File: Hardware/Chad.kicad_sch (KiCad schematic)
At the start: 39 parts, among them J1 RBUS, J2 GPIO Breakout, J3 ServoCH1, J4 ServoCH2, U1 ESP32-S3, Y1 40MHz±10ppm

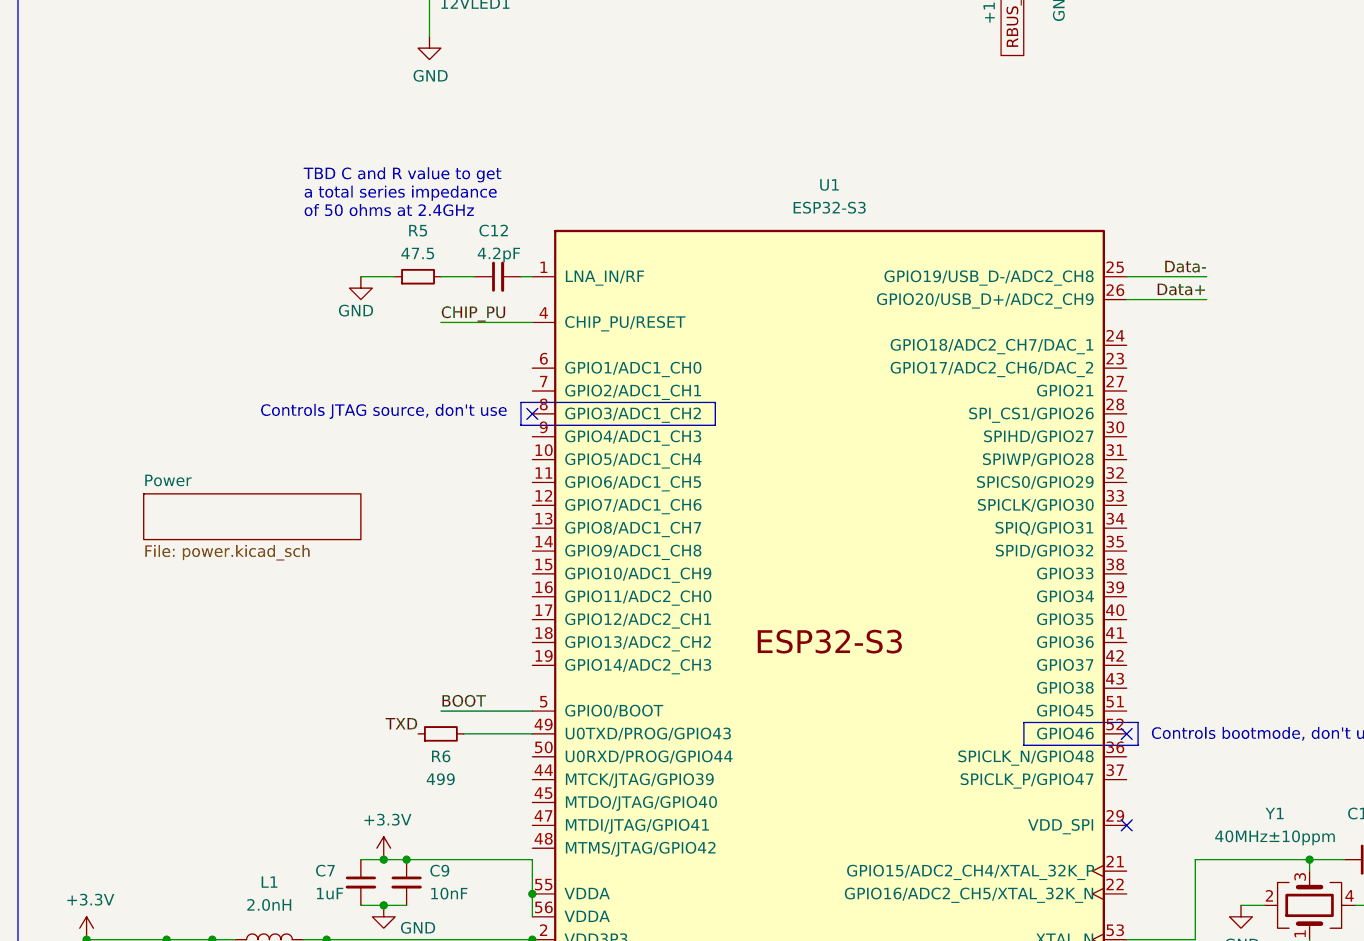
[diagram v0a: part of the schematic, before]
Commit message: Mostly completed RBUS side, still buck converter side to do
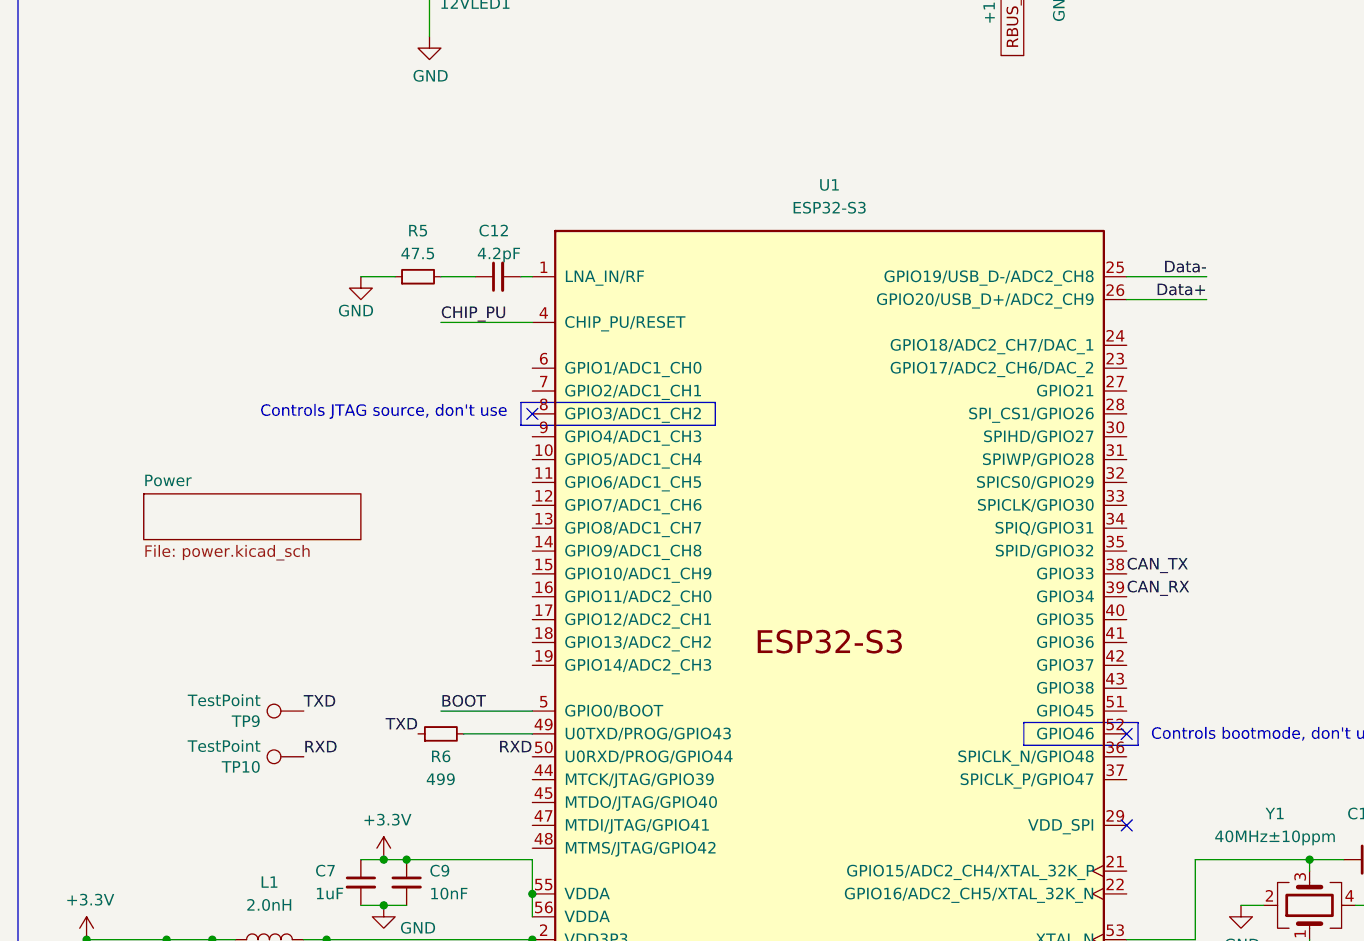
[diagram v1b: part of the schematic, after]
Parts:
- added TP10, TP9: TestPoint, TestPoint:TestPoint_Pad_D1.0mm, symbol Connector:TestPoint
- 12VLED1, 3V3LED1, TXLED1: footprint Resistor_SMD:R_0402_1005Metric -> LED_SMD:LED_0402_1005Metric
- J2: footprint (none) -> Connector_PinSocket_2.54mm:PinSocket_2x04_P2.54mm_Vertical
- U1: footprint Package_DFN_QFN:QFN-56-1EP_7x7mm_P0.4mm_EP5.6x5.6mm -> iclr:QFN40P700X700X90-57N
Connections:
- net CAN_RX: now also U1.39 (GPIO34)
- net CAN_TX: now also U1.38 (GPIO33)
- net TXD: now also TP9.1
- net RXD: now reaches U1.50 (U0RXD/PROG/GPIO44)
- net RXD: now also TP10.1
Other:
- note removed: "TBD C and R value to get a total series impedance of 50 ohms at 2.4GHz"
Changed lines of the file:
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@@
-    (effects (font (size 1.27 1.27)) (justify left bottom))
-  )
-  (text "TBD C and R value to get\na total series impedance\nof 50 ohms at 2.4GHz\n"
-    (at 44.45 55.88 0)
     (effects (font (size 1.27 1.27)) (justify left bottom))
   )
@@
     (effects (font (size 1.27 1.27)) (justify right bottom))
   )
+  (label "TXD" (at 44.45 110.49 0)
+    (effects (font (size 1.27 1.27)) (justify left bottom))
+  )
   (label "GPIO0" (at 270.51 105.41 180)
     (effects (font (size 1.27 1.27)) (justify right bottom))
@@
   (label "CHIP_PU" (at 36.83 165.1 180)
     (effects (font (size 1.27 1.27)) (justify right bottom))
+  )
+  (label "RXD" (at 44.45 115.57 0)
+    (effects (font (size 1.27 1.27)) (justify left bottom))
   )
   (label "Servo2PWM" (at 271.78 90.17 180)
@@
     (effects (font (size 1.27 1.27)) (justify right bottom))
   )
+  (label "CAN_TX" (at 135.89 95.25 0)
+    (effects (font (size 1.27 1.27)) (justify left bottom))
+  )
   (label "CHIP_PU" (at 59.69 67.31 0)
     (effects (font (size 1.27 1.27)) (justify left bottom))
   )
+  (label "RXD" (at 69.85 115.57 180)
+    (effects (font (size 1.27 1.27)) (justify right bottom))
+  )
   (label "CAN_RX" (at 115.57 182.88 0)
     (effects (font (size 1.27 1.27)) (justify left bottom))
@@
   (label "Data-" (at 144.78 62.23 180)
     (effects (font (size 1.27 1.27)) (justify right bottom))
+  )
+  (label "CAN_RX" (at 135.89 97.79 0)
+    (effects (font (size 1.27 1.27)) (justify left bottom))
   )
   (label "Servo1PWM" (at 271.78 74.93 180)
@@
     (property "Reference" "TXLED1" (id 0) (at 25.4 26.797 0))
     (property "Value" "TX_LED" (id 1) (at 25.4 24.4856 0))
-    (property "Footprint" "Resistor_SMD:R_0402_1005Metric" (id 2) (at 25.4 21.59 90)
+    (property "Footprint" "LED_SMD:LED_0402_1005Metric" (id 2) (at 25.4 21.59 90)
       (effects (font (size 1.27 1.27)) hide)
     )
@@
     (property "Reference" "3V3LED1" (id 0) (at 54.61 16.383 0))
     (property "Value" "3V3LED" (id 1) (at 54.61 18.6944 0))
-    (property "Footprint" "Resistor_SMD:R_0402_1005Metric" (id 2) (at 54.61 21.59 90)
+    (property "Footprint" "LED_SMD:LED_0402_1005Metric" (id 2) (at 54.61 21.59 90)
       (effects (font (size 1.27 1.27)) hide)
     )
@@
     (property "Reference" "12VLED1" (id 0) (at 63.5 31.877 0))
     (property "Value" "12V_LED" (id 1) (at 63.5 29.5656 0))
-    (property "Footprint" "Resistor_SMD:R_0402_1005Metric" (id 2) (at 63.5 26.67 90)
+    (property "Footprint" "LED_SMD:LED_0402_1005Metric" (id 2) (at 63.5 26.67 90)
       (effects (font (size 1.27 1.27)) hide)
     )
@@
       (effects (font (size 1.27 1.27)) (justify left))
     )
-    (property "Footprint" "" (id 2) (at 275.59 113.03 0)
+    (property "Footprint" "Connector_PinSocket_2.54mm:PinSocket_2x04_P2.54mm_Vertical" (id 2) (at 275.59 113.03 0)
       (effects (font (size 1.27 1.27)) hide)
     )
@@
     (pin "1")
   )
+  (symbol (lib_id "Connector:TestPoint") (at 44.45 110.49 90) (unit 1)
+    (in_bom yes) (on_board yes)
+    (property "Reference" "TP9" (id 0) (at 39.6748 111.6584 90)
+      (effects (font (size 1.27 1.27)) (justify left))
+    )
+    (property "Value" "TestPoint" (id 1) (at 39.6748 109.347 90)
+      (effects (font (size 1.27 1.27)) (justify left))
+    )
+    (property "Footprint" "TestPoint:TestPoint_Pad_D1.0mm" (id 2) (at 44.45 105.41 0)
+      (effects (font (size 1.27 1.27)) hide)
+    )
+    (property "Datasheet" "~" (id 3) (at 44.45 105.41 0)
+      (effects (font (size 1.27 1.27)) hide)
+    )
+    (pin "1")
+  )
   (symbol (lib_id "power:+12V") (at 120.65 25.4 180) (unit 1)
     (in_bom yes) (on_board yes)
@@
     (pin "1")
     (pin "2")
+  )
+  (symbol (lib_id "Connector:TestPoint") (at 44.45 115.57 90) (unit 1)
+    (in_bom yes) (on_board yes)
+    (property "Reference" "TP10" (id 0) (at 39.6748 116.7384 90)
+      (effects (font (size 1.27 1.27)) (justify left))
+    )
+    (property "Value" "TestPoint" (id 1) (at 39.6748 114.427 90)
+      (effects (font (size 1.27 1.27)) (justify left))
+    )
+    (property "Footprint" "TestPoint:TestPoint_Pad_D1.0mm" (id 2) (at 44.45 110.49 0)
+      (effects (font (size 1.27 1.27)) hide)
+    )
+    (property "Datasheet" "~" (id 3) (at 44.45 110.49 0)
+      (effects (font (size 1.27 1.27)) hide)
+    )
+    (pin "1")
   )
   (symbol (lib_id "Device:C_Small") (at 162.56 127 90) (unit 1)
@@
     (property "Reference" "U1" (id 0) (at 102.87 52.07 0))
     (property "Value" "ESP32-S3" (id 1) (at 102.87 54.61 0))
-    (property "Footprint" "Package_DFN_QFN:QFN-56-1EP_7x7mm_P0.4mm_EP5.6x5.6mm" (id 2) (at 102.87 153.67 0)
+    (property "Footprint" "iclr:QFN40P700X700X90-57N" (id 2) (at 102.87 153.67 0)
       (effects (font (size 1.27 1.27)) hide)
     )
@@
     )
     (path "/00000000-0000-0000-0000-00005dc1f7e5"
-      (reference "3V3LED1") (unit 1) (value "3V3LED") (footprint "Resistor_SMD:R_0402_1005Metric")
+      (reference "3V3LED1") (unit 1) (value "3V3LED") (footprint "LED_SMD:LED_0402_1005Metric")
     )
     (path "/00000000-0000-0000-0000-000061b674e8"
-      (reference "12VLED1") (unit 1) (value "12V_LED") (footprint "Resistor_SMD:R_0402_1005Metric")
+      (reference "12VLED1") (unit 1) (value "12V_LED") (footprint "LED_SMD:LED_0402_1005Metric")
     )
     (path "/00000000-0000-0000-0000-00005dff8440"
@@
     )
     (path "/00000000-0000-0000-0000-000061942b9a/c905e3f6-13b1-4d5f-8bb5-930cfa107996"
-      (reference "C17") (unit 1) (value "0.1uF") (footprint "Capacitor_SMD:C_0402_1005Metric")
+      (reference "C17") (unit 1) (value "47nF") (footprint "Capacitor_SMD:C_0402_1005Metric")
     )
     (path "/00000000-0000-0000-0000-000061942b9a/23622c20-4a70-4ee7-b39c-f5519633413f"
@@
     )
     (path "/4787afbf-a567-4e80-9253-fc8002fdff49"
-      (reference "J2") (unit 1) (value "GPIO Breakout") (footprint "")
+      (reference "J2") (unit 1) (value "GPIO Breakout") (footprint "Connector_PinSocket_2.54mm:PinSocket_2x04_P2.54mm_Vertical")
     )
     (path "/0f659bd2-aada-46fb-8f2b-6d45cea3ad46"
@@
     )
     (path "/00000000-0000-0000-0000-000061942b9a/deb2b25e-9fb0-448e-88c5-95a67db1d371"
-      (reference "JP1") (unit 1) (value "TermJP") (footprint "Jumper:SolderJumper-2_P1.3mm_Open_RoundedPad1.0x1.5mm")
+      (reference "JP1") (unit 1) (value "TermJP") (footprint "iclr:SmallerSolderJP")
     )
     (path "/c6e654d3-0d45-4a74-8557-db0239fe22b2"
@@
     )
     (path "/00000000-0000-0000-0000-000061942b9a/c4e42d16-8dbe-42af-a61a-faa72b95fe53"
-      (reference "R9") (unit 1) (value "60") (footprint "Resistor_SMD:R_0402_1005Metric")
+      (reference "R9") (unit 1) (value "60") (footprint "Resistor_SMD:R_0603_1608Metric")
     )
     (path "/00000000-0000-0000-0000-000061942b9a/c363df37-be76-44cd-846e-5e1010ee0d3e"
-      (reference "R10") (unit 1) (value "60") (footprint "Resistor_SMD:R_0402_1005Metric")
+      (reference "R10") (unit 1) (value "60") (footprint "Resistor_SMD:R_0603_1608Metric")
     )
     (path "/00000000-0000-0000-0000-000061925999/00000000-0000-0000-0000-000061988c0e"
@@
       (reference "TP2") (unit 1) (value "TestPoint") (footprint "TestPoint:TestPoint_Pad_D1.0mm")
     )
-    (path "/00000000-0000-0000-0000-000061925999/00000000-0000-0000-0000-000061ab9568"
-      (reference "TP3") (unit 1) (value "TestPoint") (footprint "TestPoint:TestPoint_Pad_D1.0mm")
-    )
     (path "/48a413b4-b7c2-44ac-971c-583c31b73475/a1c16987-99dd-46e5-b244-419050a02b4c"
       (reference "TP4") (unit 1) (value "TestPoint") (footprint "TestPoint:TestPoint_Pad_D1.5mm")
@@
       (reference "TP8") (unit 1) (value "TestPoint") (footprint "TestPoint:TestPoint_Pad_D1.5mm")
     )
+    (path "/4ef10f3b-9c72-4396-8616-41610825434e"
+      (reference "TP9") (unit 1) (value "TestPoint") (footprint "TestPoint:TestPoint_Pad_D1.0mm")
+    )
+    (path "/a1f796cf-da3c-4ed6-8b82-d103777290a5"
+      (reference "TP10") (unit 1) (value "TestPoint") (footprint "TestPoint:TestPoint_Pad_D1.0mm")
+    )
     (path "/00000000-0000-0000-0000-00005db110d6"
-      (reference "TXLED1") (unit 1) (value "TX_LED") (footprint "Resistor_SMD:R_0402_1005Metric")
+      (reference "TXLED1") (unit 1) (value "TX_LED") (footprint "LED_SMD:LED_0402_1005Metric")
     )
     (path "/c9b2ff89-c161-4200-9447-f984878121c0"
-      (reference "U1") (unit 1) (value "ESP32-S3") (footprint "Package_DFN_QFN:QFN-56-1EP_7x7mm_P0.4mm_EP5.6x5.6mm")
+      (reference "U1") (unit 1) (value "ESP32-S3") (footprint "iclr:QFN40P700X700X90-57N")
     )
     (path "/00000000-0000-0000-0000-000061942b9a/00000000-0000-0000-0000-000061946ec3"
@@
     )
     (path "/00000000-0000-0000-0000-000061925999/00000000-0000-0000-0000-000061b104ea"
-      (reference "USBLED1") (unit 1) (value "USB_LED") (footprint "Resistor_SMD:R_0402_1005Metric")
+      (reference "USBLED1") (unit 1) (value "USB_LED") (footprint "LED_SMD:LED_0402_1005Metric")
     )
     (path "/e0b09ad4-c581-4519-98b2-b00474a7d116"

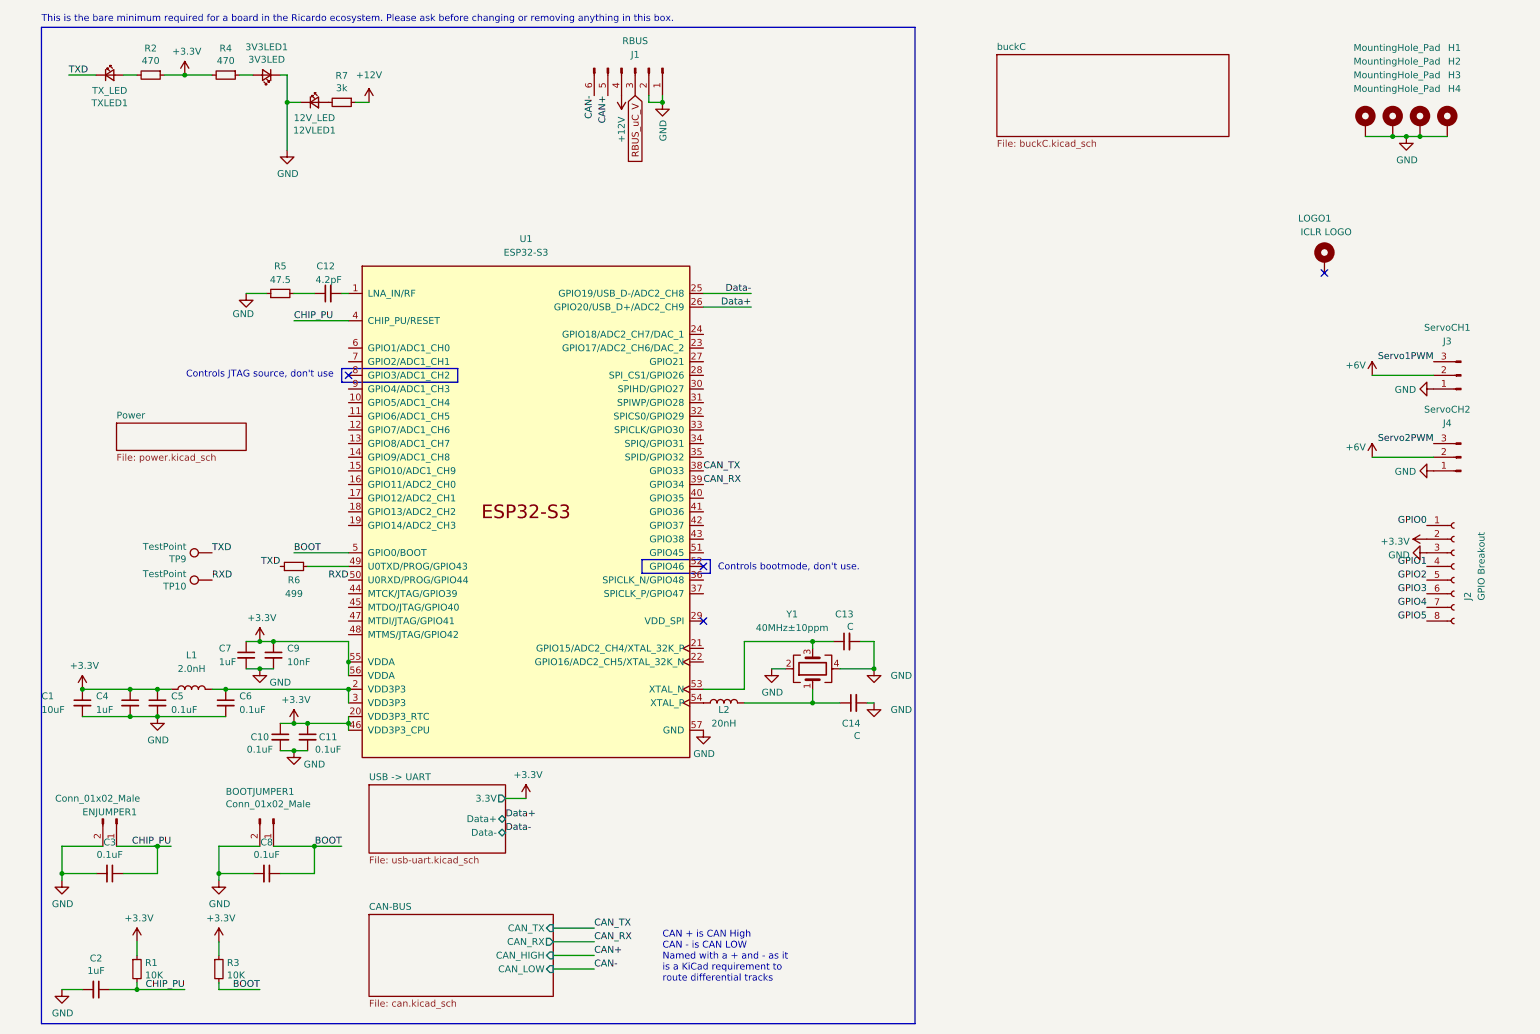
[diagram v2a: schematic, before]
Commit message: on the verge of being complete, also updated to kicad 7
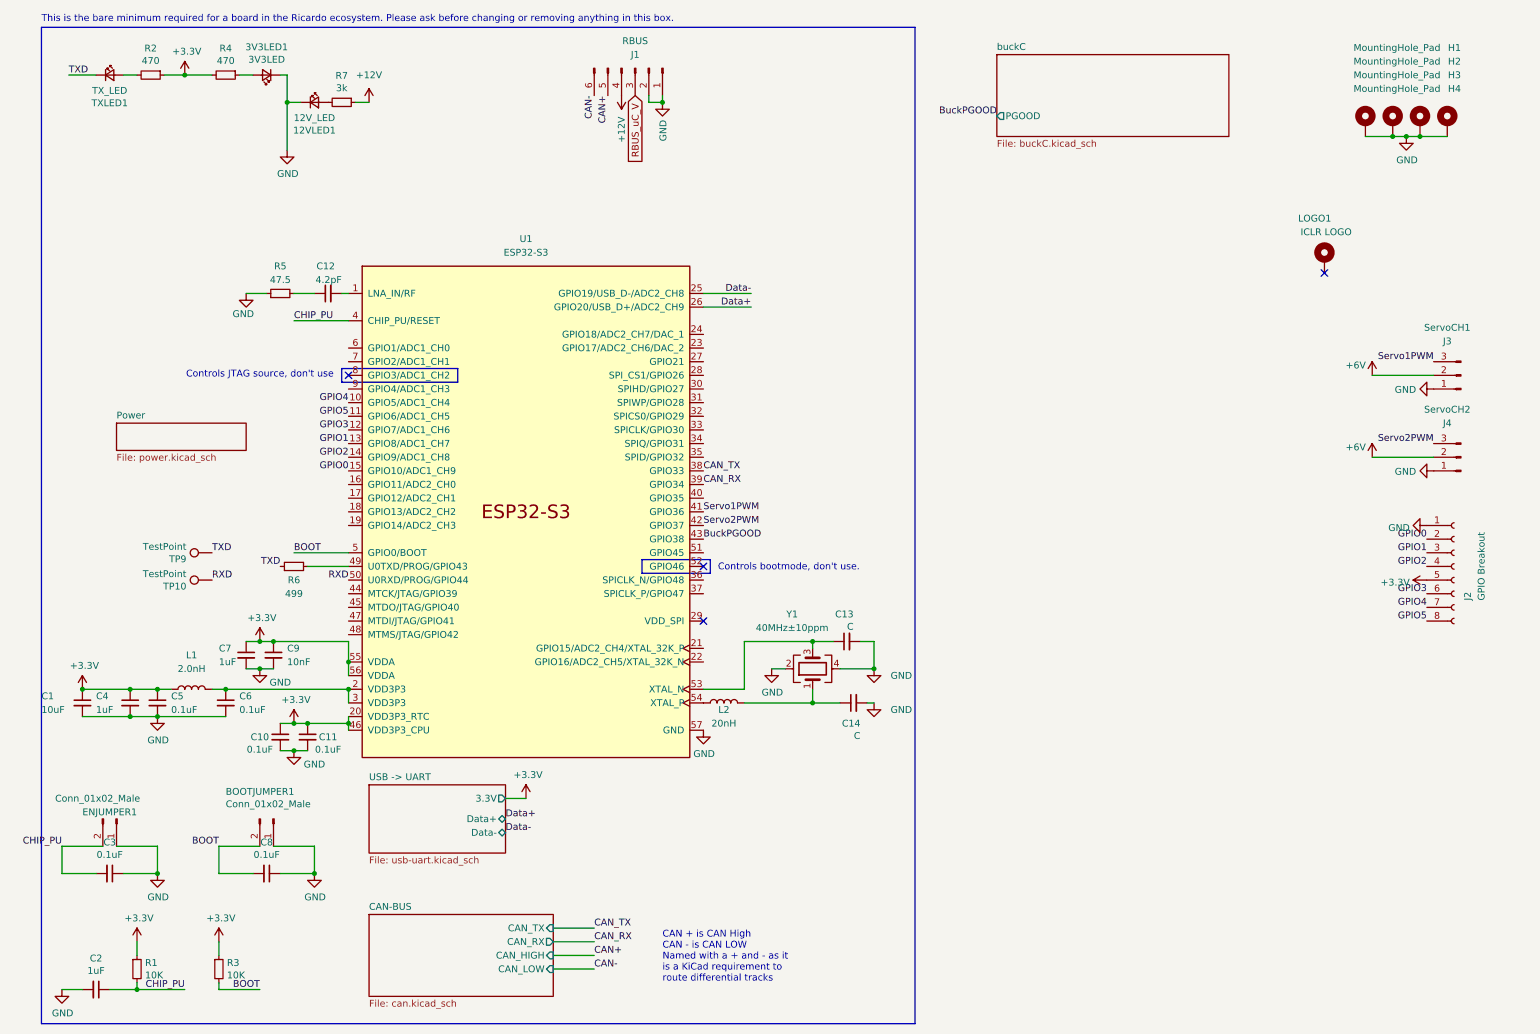
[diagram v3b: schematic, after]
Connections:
- net +3V3: now also J2.5 (Pin_5); no longer J2.2 (Pin_2)
- net BOOT: now also BOOTJUMPER1.2 (Pin_2), C8.2; no longer BOOTJUMPER1.1 (Pin_1), C8.1
- net CHIP_PU: now also C3.2, ENJUMPER1.2 (Pin_2); no longer C3.1, ENJUMPER1.1 (Pin_1)
- net GND: now also BOOTJUMPER1.1 (Pin_1), C3.1, C8.1, ENJUMPER1.1 (Pin_1), J2.1 (Pin_1); no longer BOOTJUMPER1.2 (Pin_2), C3.2, C8.2, ENJUMPER1.2 (Pin_2), J2.3 (Pin_3)
- net GPIO0: now also J2.2 (Pin_2), U1.15 (GPIO10/ADC1_CH9); no longer J2.1 (Pin_1)
- net GPIO1: now also J2.3 (Pin_3), U1.13 (GPIO8/ADC1_CH7); no longer J2.4 (Pin_4)
- net GPIO2: now also J2.4 (Pin_4), U1.14 (GPIO9/ADC1_CH8); no longer J2.5 (Pin_5)
- net GPIO3: now also U1.12 (GPIO7/ADC1_CH6)
- net GPIO4: now also U1.10 (GPIO5/ADC1_CH4)
- net GPIO5: now also U1.11 (GPIO6/ADC1_CH5)
- net Servo1PWM: now also U1.41 (GPIO36)
- net Servo2PWM: now also U1.42 (GPIO37)
- net BuckPGOOD: now reaches U1.43 (GPIO38)
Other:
- sheet buckC ports: added PGOOD; removed none
